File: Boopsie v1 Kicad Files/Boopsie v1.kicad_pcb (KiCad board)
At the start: 2 copper layers, 81 x 94.1 mm, 34 parts, among them J1 OLED_128x64, SW1 RotaryEncoder_Switch, SW2 RotaryEncoder_Switch, U1 RP2040_Zero

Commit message: final final
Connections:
- SW1 pad S1: Net-(U1-6) -> Net-(U1-5)
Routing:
- net Net-(U1-5): track 71.2 -> 121.0 mm
- net Net-(U1-6): track 117.4 -> 102.4 mm
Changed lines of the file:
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@@
 			(pintype "passive")
 		)
-		(model "${KICAD8_3DMODEL_DIR}/Rotary_Encoder.3dshapes/RotaryEncoder_Alps_EC11E-Switch_Vertical_H20mm.wrl"
+		(model "C:/Users/yogi2/Downloads/145792615-3-ec11e09244bs/ec11e09244bs.stp"
 			(offset
-				(xyz 0 0 0)
+				(xyz 7.5 -2.5 -12)
 			)
 			(scale
@@
 			)
 			(rotate
-				(xyz 0 0 0)
+				(xyz 0 180 90)
 			)
 		)
@@
 			(layers "*.Cu" "*.Mask")
 			(remove_unused_layers no)
-			(net 27 "Net-(U1-6)")
+			(net 26 "Net-(U1-5)")
 			(pinfunction "S1")
 			(pintype "passive")
@@
 			)
 		)
+		(model "C:/Users/yogi2/Downloads/145792615-3-ec11e09244bs/ec11e09244bs.stp"
+			(offset
+				(xyz 7.5 -2.5 -12.5)
+			)
+			(scale
+				(xyz 1 1 1)
+			)
+			(rotate
+				(xyz 180 0 -90)
+			)
+		)
 	)
 	(footprint "ScottoKeebs_Hotswap:Hotswap_MX_1.00u"
@@
 	)
 	(segment
+		(start 195.532576 65.343674)
+		(end 154.208674 65.343674)
+		(width 0.2)
+		(layer "F.Cu")
+		(net 26)
+	)
+	(segment
+		(start 199.345 61.53125)
+		(end 195.532576 65.343674)
+		(width 0.2)
+		(layer "F.Cu")
+		(net 26)
+	)
+	(segment
+		(start 154.208674 65.343674)
+		(end 152.04125 63.17625)
+		(width 0.2)
+		(layer "F.Cu")
+		(net 26)
+	)
+	(segment
 		(start 174.504375 74.10625)
 		(end 178.135 77.736875)
@@
 		(width 0.2)
 		(layer "B.Cu")
-		(net 27)
-	)
-	(segment
-		(start 199.345 61.53125)
-		(end 199.345 76.55)
-		(width 0.2)
-		(layer "B.Cu")

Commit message: final final final
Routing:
- net Net-(U1-5): track 121.0 -> 124.3 mm
- net Net-(U1-6): track 102.4 -> 104.3 mm
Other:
- board size 81 x 94.1 mm -> 78.6 x 90.5 mm
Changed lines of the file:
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@@
 	)
 	(gr_rect
-		(start 135.21375 38.3875)
-		(end 216.17625 132.446875)
+		(start 136.404375 39.578125)
+		(end 214.985625 130.065625)
 		(stroke
 			(width 0.05)
@@
 	)
 	(segment
-		(start 195.532576 65.343674)
-		(end 154.208674 65.343674)
+		(start 158.20875 69.34375)
+		(end 191.5325 69.34375)
 		(width 0.2)
 		(layer "F.Cu")
@@
 	)
 	(segment
-		(start 199.345 61.53125)
-		(end 195.532576 65.343674)
+		(start 152.04125 63.17625)
+		(end 158.20875 69.34375)
 		(width 0.2)
 		(layer "F.Cu")
@@
 	)
 	(segment
-		(start 154.208674 65.343674)
-		(end 152.04125 63.17625)
+		(start 191.5325 69.34375)
+		(end 199.345 61.53125)
 		(width 0.2)
 		(layer "F.Cu")
@@
 	(segment
 		(start 180.295 61.53125)
-		(end 180.295 72.753125)
+		(end 180.295 63.593135)
+		(width 0.2)
+		(layer "B.Cu")
+		(net 27)
+	)
+	(segment
+		(start 180.295 63.593135)
+		(end 189.61749 72.915625)
 		(width 0.2)
 		(layer "B.Cu")
@@
 	)
 	(segment
+		(start 189.61749 72.915625)
+		(end 190.617369 72.915625)
+		(width 0.2)
+		(layer "B.Cu")
+		(net 27)
+	)
+	(segment
 		(start 180.295 72.753125)
 		(end 180.4575 72.915625)
@@
 		(start 180.4575 72.915625)
 		(end 190.617369 72.915625)
-		(width 0.2)
-		(layer "B.Cu")
-		(net 27)
-	)
-	(segment
-		(start 199.345 76.55)
-		(end 197.185 78.71)
 		(width 0.2)
 		(layer "B.Cu")
@@
 			)
 		)
+	)
+	(zone
+		(net 0)
+		(net_name "")
+		(layers "F&B.Cu")
+		(hatch edge 0.5)
+		(priority 1)
+		(connect_pads
+			(clearance 0.5)
+		)
+		(min_thickness 0.25)
+		(filled_areas_thickness no)
+		(fill yes
+			(thermal_gap 0.5)
+			(thermal_bridge_width 0.5)
+			(island_removal_mode 1)
+			(island_area_min 10)
+		)
+		(polygon
+			(pts
+				(xy 136.404375 39.578125) (xy 214.985625 39.578125) (xy 214.985625 130.065625) (xy 136.404375 130.065625)
+			)
+		)

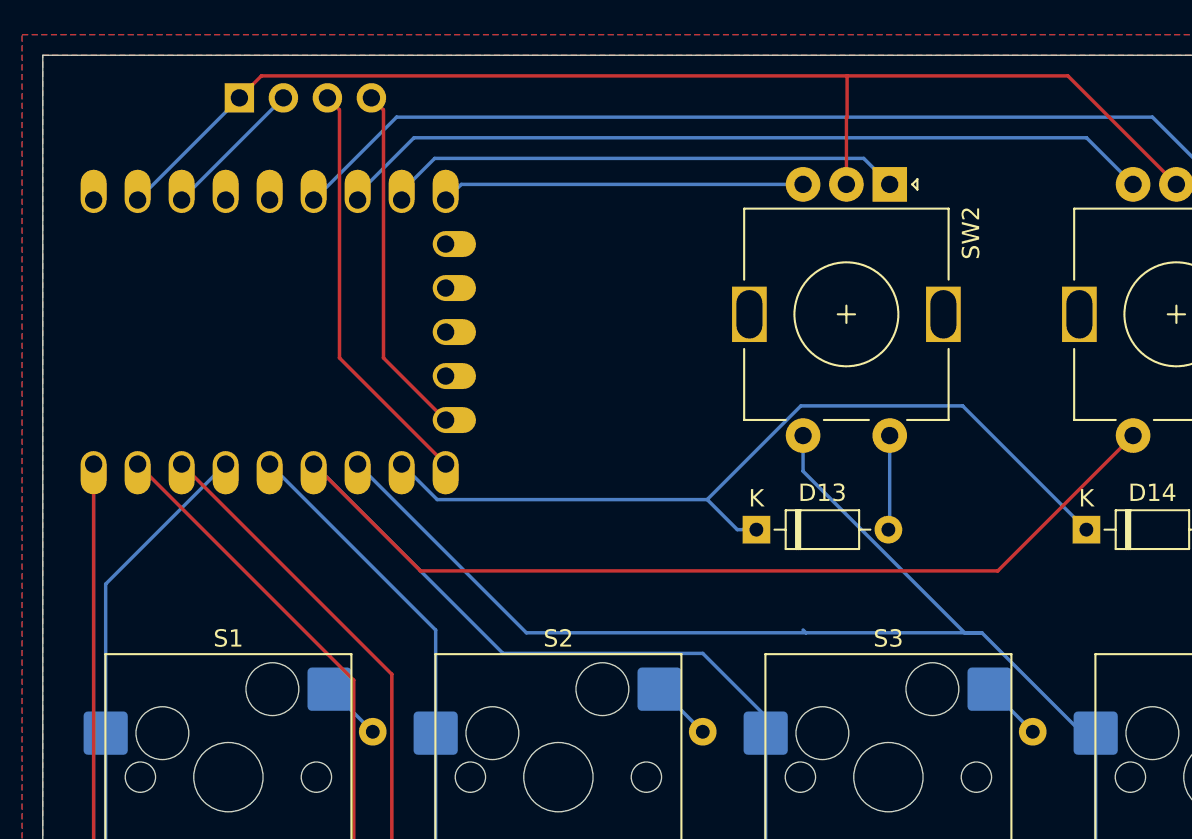
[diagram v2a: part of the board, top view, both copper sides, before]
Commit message: traces refined
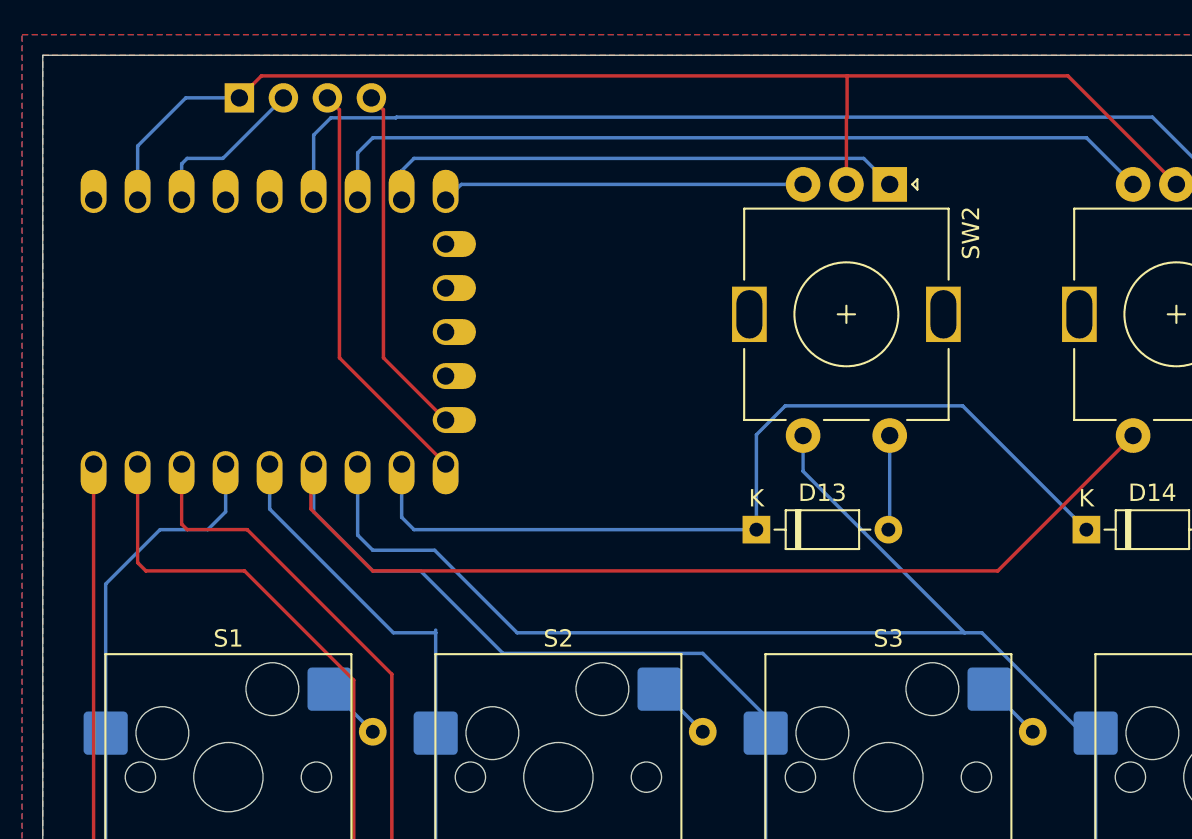
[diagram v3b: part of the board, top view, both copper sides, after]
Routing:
- net Net-(U1-5): track 124.3 -> 127.7 mm
- net Net-(D5-K): track 104.9 -> 108.2 mm
- net Net-(D13-K): track 49.1 -> 52.0 mm
- net Net-(U1-27): track 55.9 -> 58.1 mm
- net Net-(D1-K): track 85.7 -> 87.7 mm
- net Net-(J1-GND): track 71.8 -> 73.7 mm
- net Net-(U1-3): track 56.5 -> 58.1 mm
- net Net-(U1-4): track 57.6 -> 59.2 mm
- net Net-(U1-26): track 47.6 -> 49.0 mm
- net Net-(J1-VCC): track 8.33 -> 9.54 mm
- net Net-(U1-6): track 104.3 -> 105.5 mm
- net Net-(U1-15): track 30.1 -> 30.8 mm

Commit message: final trace refinement
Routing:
- net Net-(U1-4): track 59.2 -> 61.8 mm
- net Net-(U1-5): track 127.7 -> 129.7 mm
- net Net-(U1-6): track 105.5 -> 106.2 mm
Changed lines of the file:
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@@
 	)
 	(segment
-		(start 159.085 72.76)
+		(start 149.50125 70.534375)
+		(end 151.8825 72.915625)
+		(width 0.2)
+		(layer "B.Cu")
+		(net 25)
+	)
+	(segment
+		(start 149.50125 63.17625)
+		(end 149.50125 70.534375)
+		(width 0.2)
+		(layer "B.Cu")
+		(net 25)
+	)
+	(segment
+		(start 151.8825 72.915625)
 		(end 159.085 72.915625)
-		(width 0.2)
-		(layer "B.Cu")
-		(net 25)
-	)
-	(segment
-		(start 149.50125 63.17625)
-		(end 149.50125 65.771875)
-		(width 0.2)
-		(layer "B.Cu")
-		(net 25)
-	)
-	(segment
-		(start 156.645 72.915625)
-		(end 159.085 72.915625)
-		(width 0.2)
-		(layer "B.Cu")
-		(net 25)
-	)
-	(segment
-		(start 149.50125 65.771875)
-		(end 156.645 72.915625)
 		(width 0.2)
 		(layer "B.Cu")
@@
 	)
 	(segment
+		(start 178.135 77.736875)
+		(end 178.135 78.71)
+		(width 0.2)
+		(layer "B.Cu")
+		(net 26)
+	)
+	(segment
+		(start 152.04125 63.17625)
+		(end 152.04125 69.5025)
+		(width 0.2)
+		(layer "B.Cu")
+		(net 26)
+	)
+	(segment
 		(start 162.97125 74.10625)
 		(end 174.504375 74.10625)
@@
 	)
 	(segment
+		(start 154.26375 71.725)
+		(end 160.59 71.725)
+		(width 0.2)
+		(layer "B.Cu")
+		(net 26)
+	)
+	(segment
+		(start 178.135 78.71)
+		(end 178.135 116.81)
+		(width 0.2)
+		(layer "B.Cu")
+		(net 26)
+	)
+	(segment
 		(start 174.504375 74.10625)
 		(end 178.135 77.736875)
@@
 	)
 	(segment
-		(start 155.454375 69.34375)
-		(end 158.20875 69.34375)
-		(width 0.2)
-		(layer "B.Cu")
-		(net 26)
-	)
-	(segment
-		(start 152.04125 63.17625)
-		(end 152.04125 65.930625)
-		(width 0.2)
-		(layer "B.Cu")
-		(net 26)
-	)
-	(segment
-		(start 178.135 78.71)
-		(end 178.135 116.81)
-		(width 0.2)
-		(layer "B.Cu")
-		(net 26)
-	)
-	(segment
-		(start 158.20875 69.34375)
+		(start 160.59 71.725)
 		(end 162.97125 74.10625)
 		(width 0.2)
@@
 	)
 	(segment
-		(start 178.135 77.736875)
-		(end 178.135 78.71)
-		(width 0.2)
-		(layer "B.Cu")
-		(net 26)
-	)
-	(segment
-		(start 152.04125 65.930625)
-		(end 155.454375 69.34375)
-		(width 0.2)
-		(layer "B.Cu")
-		(net 26)
-	)
-	(segment
-		(start 154.58125 63.17625)
-		(end 154.58125 67.28)
-		(width 0.2)
-		(layer "B.Cu")
-		(net 27)
+		(start 152.04125 69.5025)
+		(end 154.26375 71.725)
+		(width 0.2)
+		(layer "B.Cu")
+		(net 26)
 	)
 	(segment
@@
 	)
 	(segment
-		(start 155.454375 68.153125)
-		(end 159.02625 68.153125)
-		(width 0.2)
-		(layer "B.Cu")
-		(net 27)
-	)
-	(segment
 		(start 180.295 61.53125)
 		(end 180.295 63.593135)
@@
 	)
 	(segment
+		(start 154.58125 68.470625)
+		(end 155.454375 69.34375)
+		(width 0.2)
+		(layer "B.Cu")
+		(net 27)
+	)
+	(segment
+		(start 154.58125 63.17625)
+		(end 154.58125 68.470625)
+		(width 0.2)
+		(layer "B.Cu")
+		(net 27)
+	)
+	(segment
 		(start 189.61749 72.915625)
 		(end 190.617369 72.915625)
@@
 	)
 	(segment
-		(start 154.58125 67.28)
-		(end 155.454375 68.153125)
+		(start 160.216875 69.34375)
+		(end 163.78875 72.915625)
 		(width 0.2)
 		(layer "B.Cu")
@@
 	)
 	(segment
-		(start 159.02625 68.153125)
-		(end 163.78875 72.915625)
-		(width 0.2)
-		(layer "B.Cu")
+		(start 155.454375 69.34375)
+		(end 160.216875 69.34375)
+		(width 0.2)
+		(layer "B.Cu")
